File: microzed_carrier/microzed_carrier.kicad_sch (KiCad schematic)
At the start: 2 parts, among them P1 61083-101400LF, P2 61083-101400LF

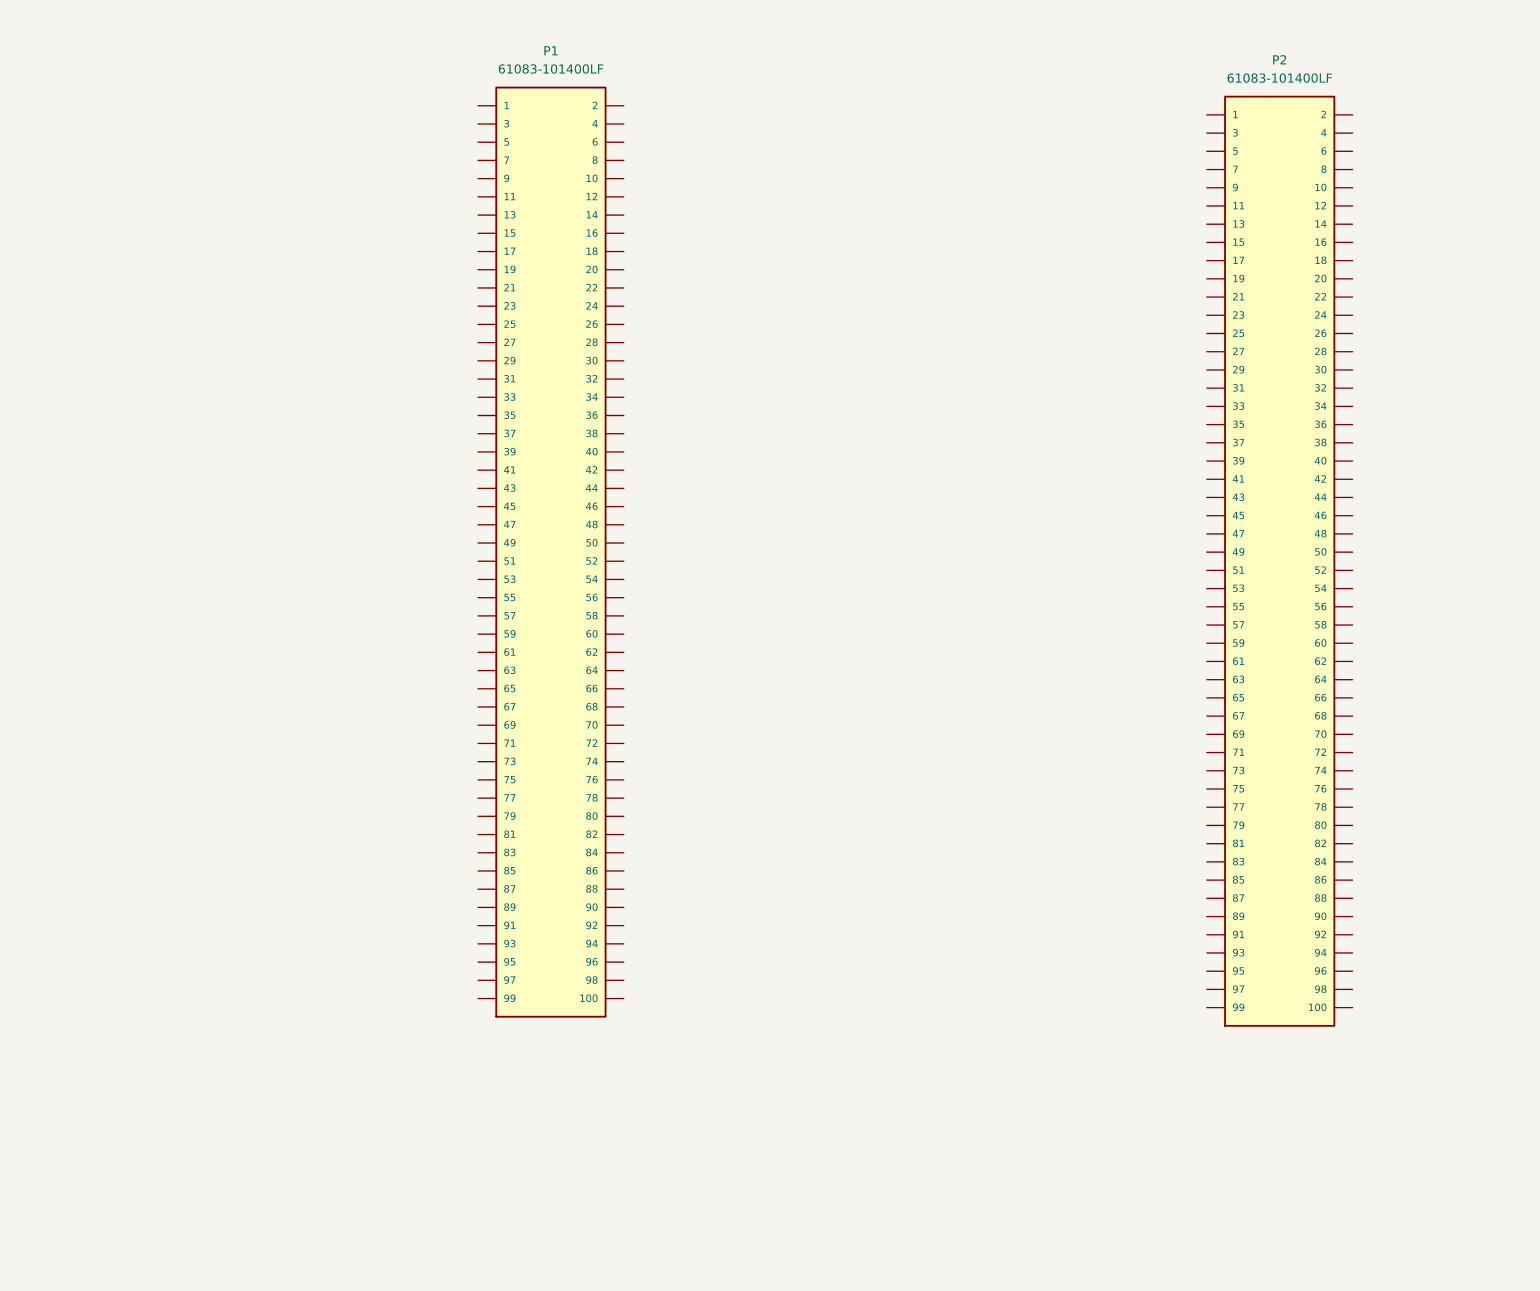
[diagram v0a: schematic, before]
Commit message: started to wire power pins on the SOM connectors
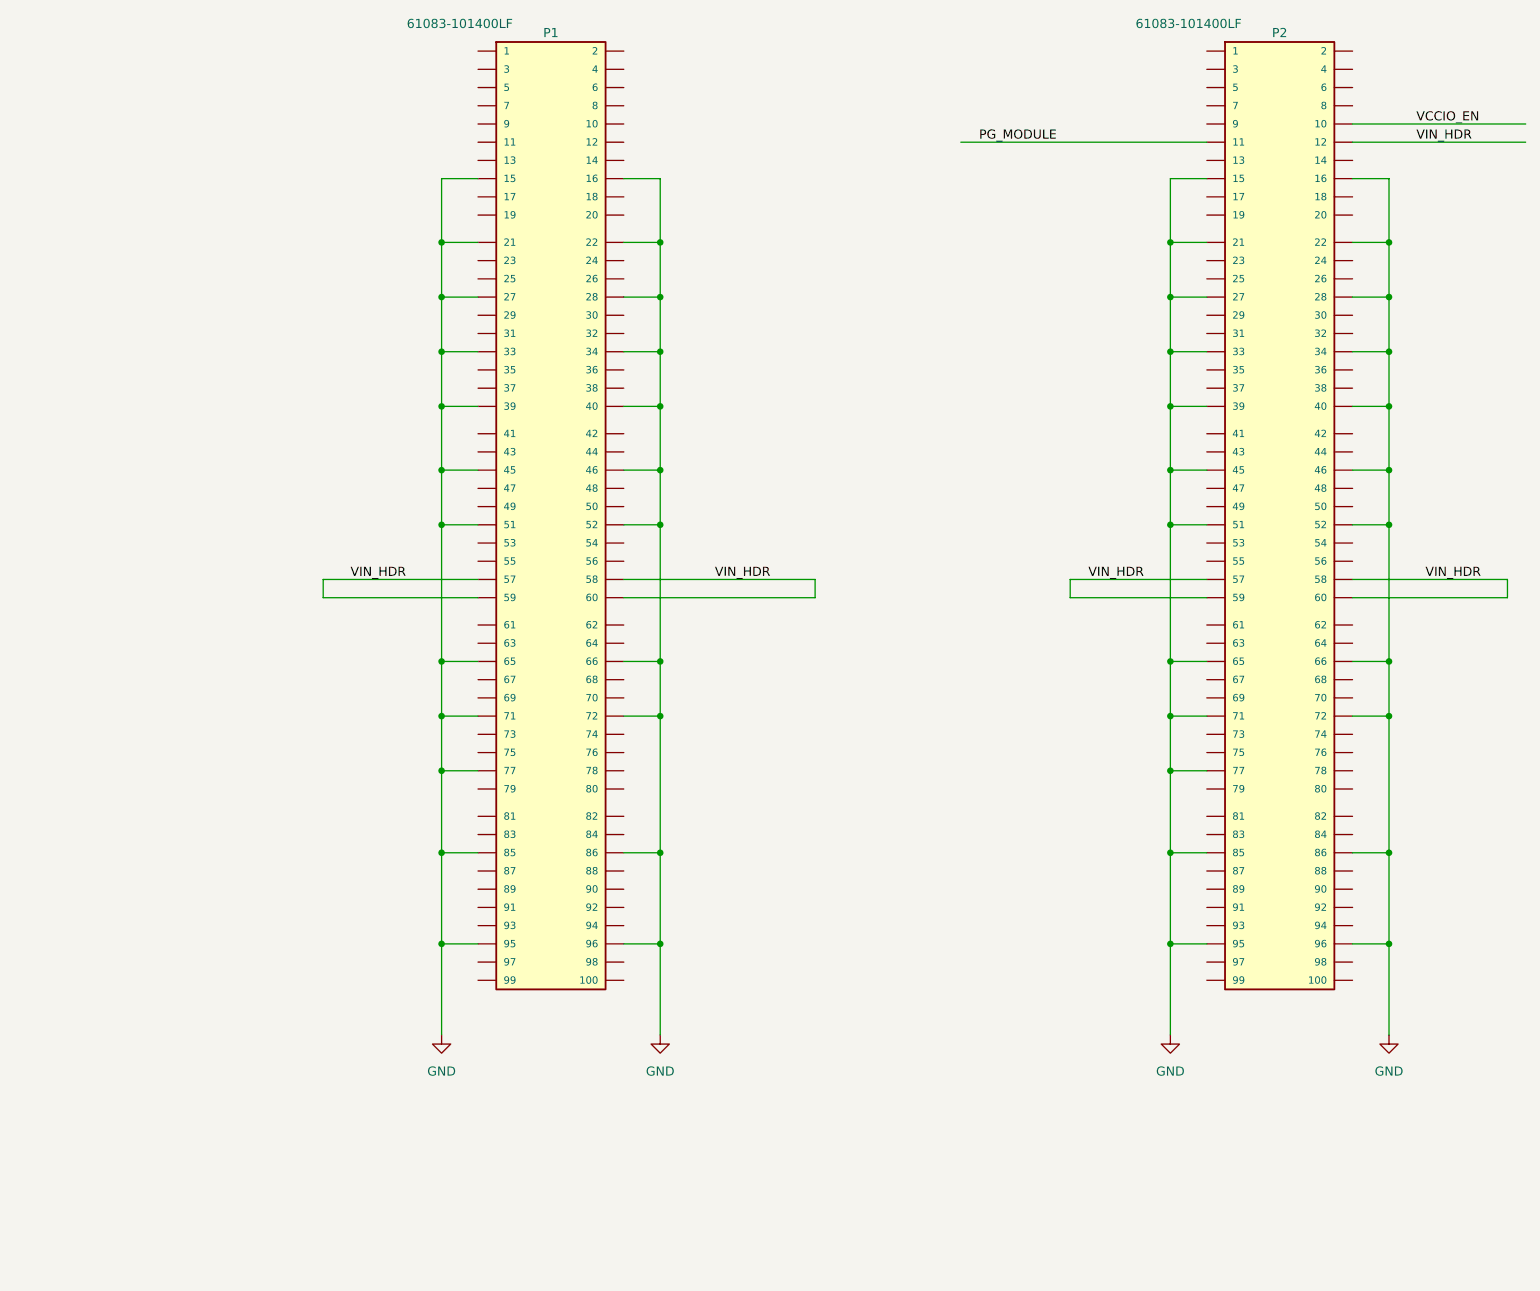
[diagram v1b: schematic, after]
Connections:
- net GND: now reaches P1.15
- net GND: now also P1.16, P1.21, P1.22, P1.27, P1.28, P1.33, P1.34, P1.39, P1.40, P1.45, P1.46, P1.51, P1.52, P1.65, P1.66, P1.71, P1.72, P1.77, P1.85, P1.86, P1.95, P1.96, P2.15, P2.16, P2.21, P2.22, P2.27, P2.28, P2.33, P2.34, P2.39, P2.40, P2.45, P2.46, P2.51, P2.52, P2.65, P2.66, P2.71, P2.72, P2.77, P2.85, P2.86, P2.95, P2.96
- net VIN_HDR: now reaches P1.57
- net VIN_HDR: now also P1.58, P1.59, P1.60, P2.12, P2.57, P2.58, P2.59, P2.60
- net VCCIO_EN: now reaches P2.10
- net PG_MODULE: now reaches P2.11
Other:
- moved on the sheet: P1, P2

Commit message: added microzed outline and mounting holes
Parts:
- added H1, H2, H3, H4: microzed_mount_hole, MountingHole:MountingHole_3.2mm_M3_Pad, symbol pedrolib:microzed_mount_hole
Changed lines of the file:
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@@
   (symbol (lib_id "power:GND") (at 110.49 158.75 0) (unit 1)
     (in_bom yes) (on_board yes) (fields_autoplaced)
-    (property "Reference" "#PWR?" (id 0) (at 110.49 165.1 0)
+    (property "Reference" "#PWR0102" (id 0) (at 110.49 165.1 0)
       (effects (font (size 1.27 1.27)) hide)
     )
@@
   (symbol (lib_id "power:GND") (at 181.61 158.75 0) (unit 1)
     (in_bom yes) (on_board yes) (fields_autoplaced)
-    (property "Reference" "#PWR?" (id 0) (at 181.61 165.1 0)
+    (property "Reference" "#PWR0103" (id 0) (at 181.61 165.1 0)
       (effects (font (size 1.27 1.27)) hide)
     )
@@
     )
     (property "Datasheet" "" (id 3) (at 181.61 158.75 0)
+      (effects (font (size 1.27 1.27)) hide)
+    )
+    (pin "1")
+  )
+  (symbol (lib_id "pedrolib:microzed_mount_hole") (at 33.02 184.15 270) (unit 1)
+    (in_bom yes) (on_board yes) (fields_autoplaced)
+    (property "Reference" "H4" (id 0) (at 36.83 182.8799 90)
+      (effects (font (size 1.27 1.27)) (justify left))
+    )
+    (property "Value" "microzed_mount_hole" (id 1) (at 36.83 185.4199 90)
+      (effects (font (size 1.27 1.27)) (justify left))
+    )
+    (property "Footprint" "MountingHole:MountingHole_3.2mm_M3_Pad" (id 2) (at 33.02 184.15 0)
+      (effects (font (size 1.27 1.27)) hide)
+    )
+    (property "Datasheet" "~" (id 3) (at 33.02 184.15 0)
       (effects (font (size 1.27 1.27)) hide)
     )
@@
   (symbol (lib_id "power:GND") (at 80.01 158.75 0) (unit 1)
     (in_bom yes) (on_board yes) (fields_autoplaced)
-    (property "Reference" "#PWR?" (id 0) (at 80.01 165.1 0)
+    (property "Reference" "#PWR0101" (id 0) (at 80.01 165.1 0)
       (effects (font (size 1.27 1.27)) hide)
     )
@@
   (symbol (lib_id "power:GND") (at 212.09 158.75 0) (unit 1)
     (in_bom yes) (on_board yes) (fields_autoplaced)
-    (property "Reference" "#PWR?" (id 0) (at 212.09 165.1 0)
+    (property "Reference" "#PWR0104" (id 0) (at 212.09 165.1 0)
       (effects (font (size 1.27 1.27)) hide)
     )
@@
     )
     (property "Datasheet" "" (id 3) (at 212.09 158.75 0)
+      (effects (font (size 1.27 1.27)) hide)
+    )
+    (pin "1")
+  )
+  (symbol (lib_id "pedrolib:microzed_mount_hole") (at 33.02 173.99 270) (unit 1)
+    (in_bom yes) (on_board yes) (fields_autoplaced)
+    (property "Reference" "H2" (id 0) (at 36.83 172.7199 90)
+      (effects (font (size 1.27 1.27)) (justify left))
+    )
+    (property "Value" "microzed_mount_hole" (id 1) (at 36.83 175.2599 90)
+      (effects (font (size 1.27 1.27)) (justify left))
+    )
+    (property "Footprint" "MountingHole:MountingHole_3.2mm_M3_Pad" (id 2) (at 33.02 173.99 0)
+      (effects (font (size 1.27 1.27)) hide)
+    )
+    (property "Datasheet" "~" (id 3) (at 33.02 173.99 0)
+      (effects (font (size 1.27 1.27)) hide)
+    )
+    (pin "1")
+  )
+  (symbol (lib_id "pedrolib:microzed_mount_hole") (at 33.02 179.07 270) (unit 1)
+    (in_bom yes) (on_board yes) (fields_autoplaced)
+    (property "Reference" "H1" (id 0) (at 36.83 177.7999 90)
+      (effects (font (size 1.27 1.27)) (justify left))
+    )
+    (property "Value" "microzed_mount_hole" (id 1) (at 36.83 180.3399 90)
+      (effects (font (size 1.27 1.27)) (justify left))
+    )
+    (property "Footprint" "MountingHole:MountingHole_3.2mm_M3_Pad" (id 2) (at 33.02 179.07 0)
+      (effects (font (size 1.27 1.27)) hide)
+    )
+    (property "Datasheet" "~" (id 3) (at 33.02 179.07 0)
+      (effects (font (size 1.27 1.27)) hide)
+    )
+    (pin "1")
+  )
+  (symbol (lib_id "pedrolib:microzed_mount_hole") (at 33.02 189.23 270) (unit 1)
+    (in_bom yes) (on_board yes) (fields_autoplaced)
+    (property "Reference" "H3" (id 0) (at 36.83 187.9599 90)
+      (effects (font (size 1.27 1.27)) (justify left))
+    )
+    (property "Value" "microzed_mount_hole" (id 1) (at 36.83 190.4999 90)
+      (effects (font (size 1.27 1.27)) (justify left))
+    )
+    (property "Footprint" "MountingHole:MountingHole_3.2mm_M3_Pad" (id 2) (at 33.02 189.23 0)
+      (effects (font (size 1.27 1.27)) hide)
+    )
+    (property "Datasheet" "~" (id 3) (at 33.02 189.23 0)
       (effects (font (size 1.27 1.27)) hide)
     )
@@
   )
   (symbol_instances
+    (path "/3322a943-b864-4f87-baf5-9a9a2a73b092"
+      (reference "#PWR0101") (unit 1) (value "GND") (footprint "")
+    )
     (path "/0c147b9f-8740-4faa-b461-7d3b93bcd821"
-      (reference "#PWR?") (unit 1) (value "GND") (footprint "")
+      (reference "#PWR0102") (unit 1) (value "GND") (footprint "")
     )
     (path "/0cc719dd-8844-40cf-aa49-b972d9434f32"
-      (reference "#PWR?") (unit 1) (value "GND") (footprint "")
-    )
-    (path "/3322a943-b864-4f87-baf5-9a9a2a73b092"
-      (reference "#PWR?") (unit 1) (value "GND") (footprint "")
+      (reference "#PWR0103") (unit 1) (value "GND") (footprint "")
     )
     (path "/97dbc59a-30e8-4f91-94d9-8a10ba811402"
-      (reference "#PWR?") (unit 1) (value "GND") (footprint "")
+      (reference "#PWR0104") (unit 1) (value "GND") (footprint "")
+    )
+    (path "/e4d458ff-649f-47c6-a633-a1ea2ad4bb80"
+      (reference "H1") (unit 1) (value "microzed_mount_hole") (footprint "MountingHole:MountingHole_3.2mm_M3_Pad")
+    )
+    (path "/a58a3a7c-23bb-4db0-b7c5-2b9c7b3a2043"
+      (reference "H2") (unit 1) (value "microzed_mount_hole") (footprint "MountingHole:MountingHole_3.2mm_M3_Pad")
+    )
+    (path "/ee960be5-d169-4db3-9d1b-775cdaea27ae"
+      (reference "H3") (unit 1) (value "microzed_mount_hole") (footprint "MountingHole:MountingHole_3.2mm_M3_Pad")
+    )
+    (path "/1c8493d2-66a5-4600-aa0b-7a2f733f8735"
+      (reference "H4") (unit 1) (value "microzed_mount_hole") (footprint "MountingHole:MountingHole_3.2mm_M3_Pad")
     )
     (path "/2f0771ac-785e-49cd-b5db-9060c3cbc2f1"

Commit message: added mounting holes and some LEDs
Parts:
- added D1, D2, D3, D4: LED, LED_SMD:LED_0603_1608Metric, symbol Device:LED
- added J1: Jack-DC, Connector_BarrelJack:BarrelJack_CLIFF_FC681465S_SMT_Horizontal, symbol Connector:Jack-DC
- added R1, R2, R3, R4: R, Resistor_SMD:R_0603_1608Metric, symbol Device:R
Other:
- note added: "SOM Connectors"
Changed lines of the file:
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@@
     (stroke (width 0) (type default) (color 0 0 0 0))
+  )
+  (text "SOM Connectors" (at 187.96 191.77 0)
+    (effects (font (size 2 2)) (justify left bottom))
   )
   (label "VIN_HDR" (at 118.11 95.25 0)
@@
     (pin "1")
   )
+  (symbol (lib_id "Device:LED") (at 49.53 69.85 0) (unit 1)
+    (in_bom yes) (on_board yes) (fields_autoplaced)
+    (property "Reference" "D4" (id 0) (at 47.9425 63.5 0))
+    (property "Value" "LED" (id 1) (at 47.9425 66.04 0))
+    (property "Footprint" "LED_SMD:LED_0603_1608Metric" (id 2) (at 49.53 69.85 0)
+      (effects (font (size 1.27 1.27)) hide)
+    )
+    (property "Datasheet" "~" (id 3) (at 49.53 69.85 0)
+      (effects (font (size 1.27 1.27)) hide)
+    )
+    (pin "1")
+    (pin "2")
+  )
   (symbol (lib_id "pedrolib:microzed_mount_hole") (at 33.02 184.15 270) (unit 1)
     (in_bom yes) (on_board yes) (fields_autoplaced)
@@
     )
     (pin "1")
+  )
+  (symbol (lib_id "Device:R") (at 30.48 132.08 0) (unit 1)
+    (in_bom yes) (on_board yes) (fields_autoplaced)
+    (property "Reference" "R2" (id 0) (at 33.02 130.8099 0)
+      (effects (font (size 1.27 1.27)) (justify left))
+    )
+    (property "Value" "R" (id 1) (at 33.02 133.3499 0)
+      (effects (font (size 1.27 1.27)) (justify left))
+    )
+    (property "Footprint" "Resistor_SMD:R_0603_1608Metric" (id 2) (at 28.702 132.08 90)
+      (effects (font (size 1.27 1.27)) hide)
+    )
+    (property "Datasheet" "~" (id 3) (at 30.48 132.08 0)
+      (effects (font (size 1.27 1.27)) hide)
+    )
+    (pin "1")
+    (pin "2")
   )
   (symbol (lib_name "61083-101400LF_1") (lib_id "pedrolib:61083-101400LF") (at 95.25 87.63 0) (unit 1)
@@
     (pin "1")
   )
+  (symbol (lib_id "Connector:Jack-DC") (at 72.39 185.42 0) (unit 1)
+    (in_bom yes) (on_board yes) (fields_autoplaced)
+    (property "Reference" "J1" (id 0) (at 72.39 176.53 0))
+    (property "Value" "Jack-DC" (id 1) (at 72.39 179.07 0))
+    (property "Footprint" "Connector_BarrelJack:BarrelJack_CLIFF_FC681465S_SMT_Horizontal" (id 2) (at 73.66 186.436 0)
+      (effects (font (size 1.27 1.27)) hide)
+    )
+    (property "Datasheet" "~" (id 3) (at 73.66 186.436 0)
+      (effects (font (size 1.27 1.27)) hide)
+    )
+    (pin "1")
+    (pin "2")
+  )
   (symbol (lib_id "pedrolib:microzed_mount_hole") (at 33.02 173.99 270) (unit 1)
     (in_bom yes) (on_board yes) (fields_autoplaced)
@@
     (pin "1")
   )
+  (symbol (lib_id "Device:LED") (at 33.02 55.88 0) (unit 1)
+    (in_bom yes) (on_board yes) (fields_autoplaced)
+    (property "Reference" "D3" (id 0) (at 31.4325 49.53 0))
+    (property "Value" "LED" (id 1) (at 31.4325 52.07 0))
+    (property "Footprint" "LED_SMD:LED_0603_1608Metric" (id 2) (at 33.02 55.88 0)
+      (effects (font (size 1.27 1.27)) hide)
+    )
+    (property "Datasheet" "~" (id 3) (at 33.02 55.88 0)
+      (effects (font (size 1.27 1.27)) hide)
+    )
+    (pin "1")
+    (pin "2")
+  )
+  (symbol (lib_id "Device:R") (at 21.59 148.59 0) (unit 1)
+    (in_bom yes) (on_board yes) (fields_autoplaced)
+    (property "Reference" "R1" (id 0) (at 24.13 147.3199 0)
+      (effects (font (size 1.27 1.27)) (justify left))
+    )
+    (property "Value" "R" (id 1) (at 24.13 149.8599 0)
+      (effects (font (size 1.27 1.27)) (justify left))
+    )
+    (property "Footprint" "Resistor_SMD:R_0603_1608Metric" (id 2) (at 19.812 148.59 90)
+      (effects (font (size 1.27 1.27)) hide)
+    )
+    (property "Datasheet" "~" (id 3) (at 21.59 148.59 0)
+      (effects (font (size 1.27 1.27)) hide)
+    )
+    (pin "1")
+    (pin "2")
+  )
+  (symbol (lib_id "Device:LED") (at 30.48 106.68 0) (unit 1)
+    (in_bom yes) (on_board yes) (fields_autoplaced)
+    (property "Reference" "D1" (id 0) (at 28.8925 100.33 0))
+    (property "Value" "LED" (id 1) (at 28.8925 102.87 0))
+    (property "Footprint" "LED_SMD:LED_0603_1608Metric" (id 2) (at 30.48 106.68 0)
+      (effects (font (size 1.27 1.27)) hide)
+    )
+    (property "Datasheet" "~" (id 3) (at 30.48 106.68 0)
+      (effects (font (size 1.27 1.27)) hide)
+    )
+    (pin "1")
+    (pin "2")
+  )
+  (symbol (lib_id "Device:LED") (at 31.75 83.82 0) (unit 1)
+    (in_bom yes) (on_board yes) (fields_autoplaced)
+    (property "Reference" "D2" (id 0) (at 30.1625 77.47 0))
+    (property "Value" "LED" (id 1) (at 30.1625 80.01 0))
+    (property "Footprint" "LED_SMD:LED_0603_1608Metric" (id 2) (at 31.75 83.82 0)
+      (effects (font (size 1.27 1.27)) hide)
+    )
+    (property "Datasheet" "~" (id 3) (at 31.75 83.82 0)
+      (effects (font (size 1.27 1.27)) hide)
+    )
+    (pin "1")
+    (pin "2")
+  )
+  (symbol (lib_id "Device:R") (at 38.1 123.19 0) (unit 1)
+    (in_bom yes) (on_board yes) (fields_autoplaced)
+    (property "Reference" "R4" (id 0) (at 40.64 121.9199 0)
+      (effects (font (size 1.27 1.27)) (justify left))
+    )
+    (property "Value" "R" (id 1) (at 40.64 124.4599 0)
+      (effects (font (size 1.27 1.27)) (justify left))
+    )
+    (property "Footprint" "Resistor_SMD:R_0603_1608Metric" (id 2) (at 36.322 123.19 90)
+      (effects (font (size 1.27 1.27)) hide)
+    )
+    (property "Datasheet" "~" (id 3) (at 38.1 123.19 0)
+      (effects (font (size 1.27 1.27)) hide)
+    )
+    (pin "1")
+    (pin "2")
+  )
   (symbol (lib_id "pedrolib:microzed_mount_hole") (at 33.02 179.07 270) (unit 1)
     (in_bom yes) (on_board yes) (fields_autoplaced)
@@
     )
     (pin "1")
+  )
+  (symbol (lib_id "Device:R") (at 35.56 148.59 0) (unit 1)
+    (in_bom yes) (on_board yes) (fields_autoplaced)
+    (property "Reference" "R3" (id 0) (at 38.1 147.3199 0)
+      (effects (font (size 1.27 1.27)) (justify left))
+    )
+    (property "Value" "R" (id 1) (at 38.1 149.8599 0)
+      (effects (font (size 1.27 1.27)) (justify left))
+    )
+    (property "Footprint" "Resistor_SMD:R_0603_1608Metric" (id 2) (at 33.782 148.59 90)
+      (effects (font (size 1.27 1.27)) hide)
+    )
+    (property "Datasheet" "~" (id 3) (at 35.56 148.59 0)
+      (effects (font (size 1.27 1.27)) hide)
+    )
+    (pin "1")
+    (pin "2")
   )
   (symbol (lib_id "pedrolib:61083-101400LF") (at 196.85 87.63 0) (unit 1)
@@
       (reference "#PWR0104") (unit 1) (value "GND") (footprint "")
     )
+    (path "/cd56e84d-19b5-4adb-9f5b-1fb59509eb6c"
+      (reference "D1") (unit 1) (value "LED") (footprint "LED_SMD:LED_0603_1608Metric")
+    )
+    (path "/cf36bd52-010b-4462-a0d8-14a6752d3036"
+      (reference "D2") (unit 1) (value "LED") (footprint "LED_SMD:LED_0603_1608Metric")
+    )
+    (path "/b292607f-c4c8-4dd9-a1b6-46e30919b592"
+      (reference "D3") (unit 1) (value "LED") (footprint "LED_SMD:LED_0603_1608Metric")
+    )
+    (path "/14a896c8-4bfb-43b2-9121-1f783c5a2dd5"
+      (reference "D4") (unit 1) (value "LED") (footprint "LED_SMD:LED_0603_1608Metric")
+    )
     (path "/e4d458ff-649f-47c6-a633-a1ea2ad4bb80"
       (reference "H1") (unit 1) (value "microzed_mount_hole") (footprint "MountingHole:MountingHole_3.2mm_M3_Pad")
@@
       (reference "H4") (unit 1) (value "microzed_mount_hole") (footprint "MountingHole:MountingHole_3.2mm_M3_Pad")
     )
+    (path "/9fc6d450-5606-44ce-83b3-99d14ffbb0fb"
+      (reference "J1") (unit 1) (value "Jack-DC") (footprint "Connector_BarrelJack:BarrelJack_CLIFF_FC681465S_SMT_Horizontal")
+    )
     (path "/2f0771ac-785e-49cd-b5db-9060c3cbc2f1"
       (reference "P1") (unit 1) (value "61083-101400LF") (footprint "pedrolib:FCI_61083-101400LF")
@@
       (reference "P2") (unit 1) (value "61083-101400LF") (footprint "pedrolib:FCI_61083-101400LF")
     )
-  )
+    (path "/bc9b2c5e-8d9d-40c0-aade-26b8bc707387"
+      (reference "R1") (unit 1) (value "R") (footprint "Resistor_SMD:R_0603_1608Metric")
+    )
+    (path "/23c7f802-77fb-4efa-b504-a7b924d702dd"
+      (reference "R2") (unit 1) (value "R") (footprint "Resistor_SMD:R_0603_1608Metric")
+    )
+    (path "/f07d119a-c99d-4aeb-85b8-cde009ce458c"
+      (reference "R3") (unit 1) (value "R") (footprint "Resistor_SMD:R_0603_1608Metric")
+    )
+    (path "/e1c5c0e3-dba3-46a2-af78-f33a30a88b11"
+      (reference "R4") (unit 1) (value "R") (footprint "Resistor_SMD:R_0603_1608Metric")
+    )
+  )
